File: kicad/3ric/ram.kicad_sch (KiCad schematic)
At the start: 7 parts

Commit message: update schematics
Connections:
- net CD0: now also U_BUS_DATA_?.18 (B0); no longer U_BUS_DATA_?.2 (A0)
- net CD1: now also U_BUS_DATA_?.17 (B1); no longer U_BUS_DATA_?.3 (A1)
- net CD2: now also U_BUS_DATA_?.16 (B2); no longer U_BUS_DATA_?.4 (A2)
- net CD3: now also U_BUS_DATA_?.15 (B3); no longer U_BUS_DATA_?.5 (A3)
- net CD4: now also U_BUS_DATA_?.14 (B4); no longer U_BUS_DATA_?.6 (A4)
- net CD5: now also U_BUS_DATA_?.13 (B5); no longer U_BUS_DATA_?.7 (A5)
- net CD6: now also U_BUS_DATA_?.12 (B6); no longer U_BUS_DATA_?.8 (A6)
- net CD7: now also U_BUS_DATA_?.11 (B7); no longer U_BUS_DATA_?.9 (A7)
- net VD0: now also U_BUS_DATA_?.2 (A0); no longer U_BUS_DATA_?.18 (B0)
- net VD1: now also U_BUS_DATA_?.3 (A1); no longer U_BUS_DATA_?.17 (B1)
- net VD2: now also U_BUS_DATA_?.4 (A2); no longer U_BUS_DATA_?.16 (B2)
- net VD3: now also U_BUS_DATA_?.5 (A3); no longer U_BUS_DATA_?.15 (B3)
- net VD4: now also U_BUS_DATA_?.6 (A4); no longer U_BUS_DATA_?.14 (B4)
- net VD5: now also U_BUS_DATA_?.7 (A5); no longer U_BUS_DATA_?.13 (B5)
- net VD6: now also U_BUS_DATA_?.8 (A6); no longer U_BUS_DATA_?.12 (B6)
- net VD7: now also U_BUS_DATA_?.9 (A7); no longer U_BUS_DATA_?.11 (B7)
- net VL0: now also U_VDATA_LATCH?.19 (Q0); no longer U_VDATA_LATCH?.12 (Q7)
- net VL1: now also U_VDATA_LATCH?.18 (Q1); no longer U_VDATA_LATCH?.13 (Q6)
- net VL2: now also U_VDATA_LATCH?.17 (Q2); no longer U_VDATA_LATCH?.14 (Q5)
- net VL3: now also U_VDATA_LATCH?.16 (Q3); no longer U_VDATA_LATCH?.15 (Q4)
- net VL4: now also U_VDATA_LATCH?.15 (Q4); no longer U_VDATA_LATCH?.16 (Q3)
- net VL5: now also U_VDATA_LATCH?.14 (Q5); no longer U_VDATA_LATCH?.17 (Q2)
- net VL6: now also U_VDATA_LATCH?.13 (Q6); no longer U_VDATA_LATCH?.18 (Q1)
- net VL7: now also U_VDATA_LATCH?.12 (Q7); no longer U_VDATA_LATCH?.19 (Q0)
- net VIDENABLE renamed VIDENABLE2

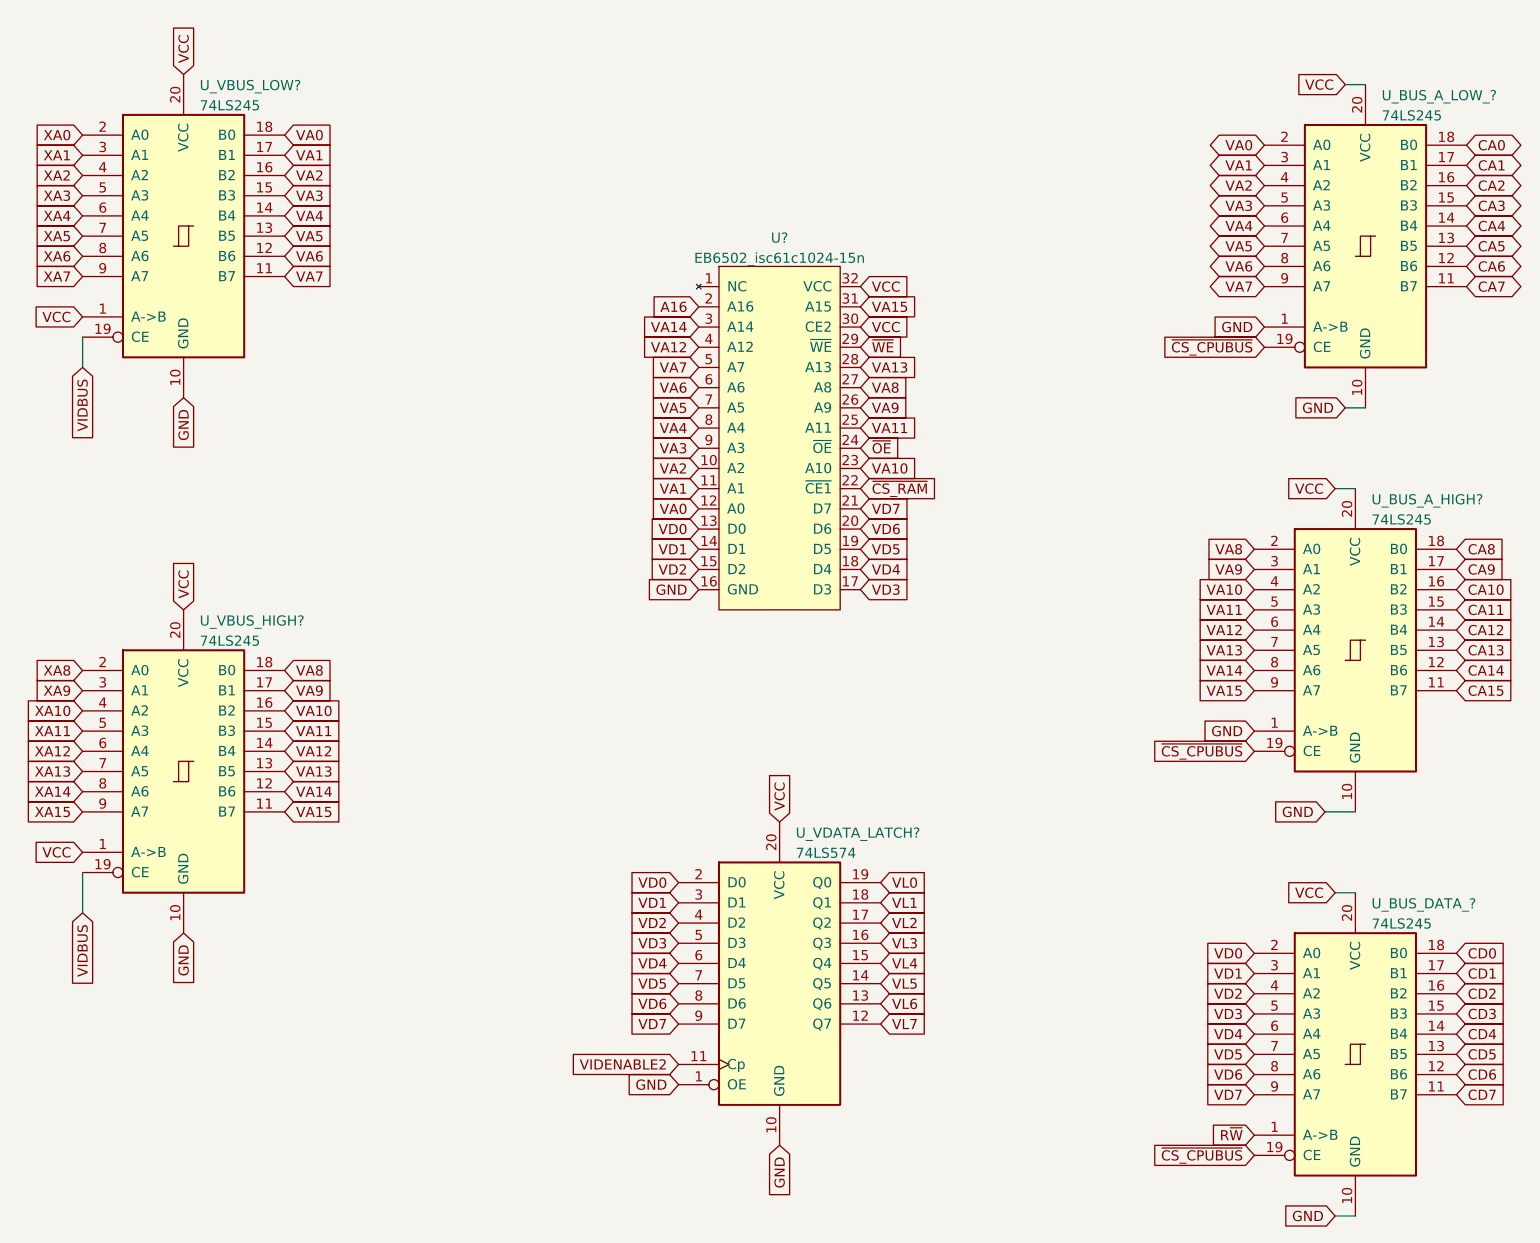
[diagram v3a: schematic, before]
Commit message: update schematic based on breadboard
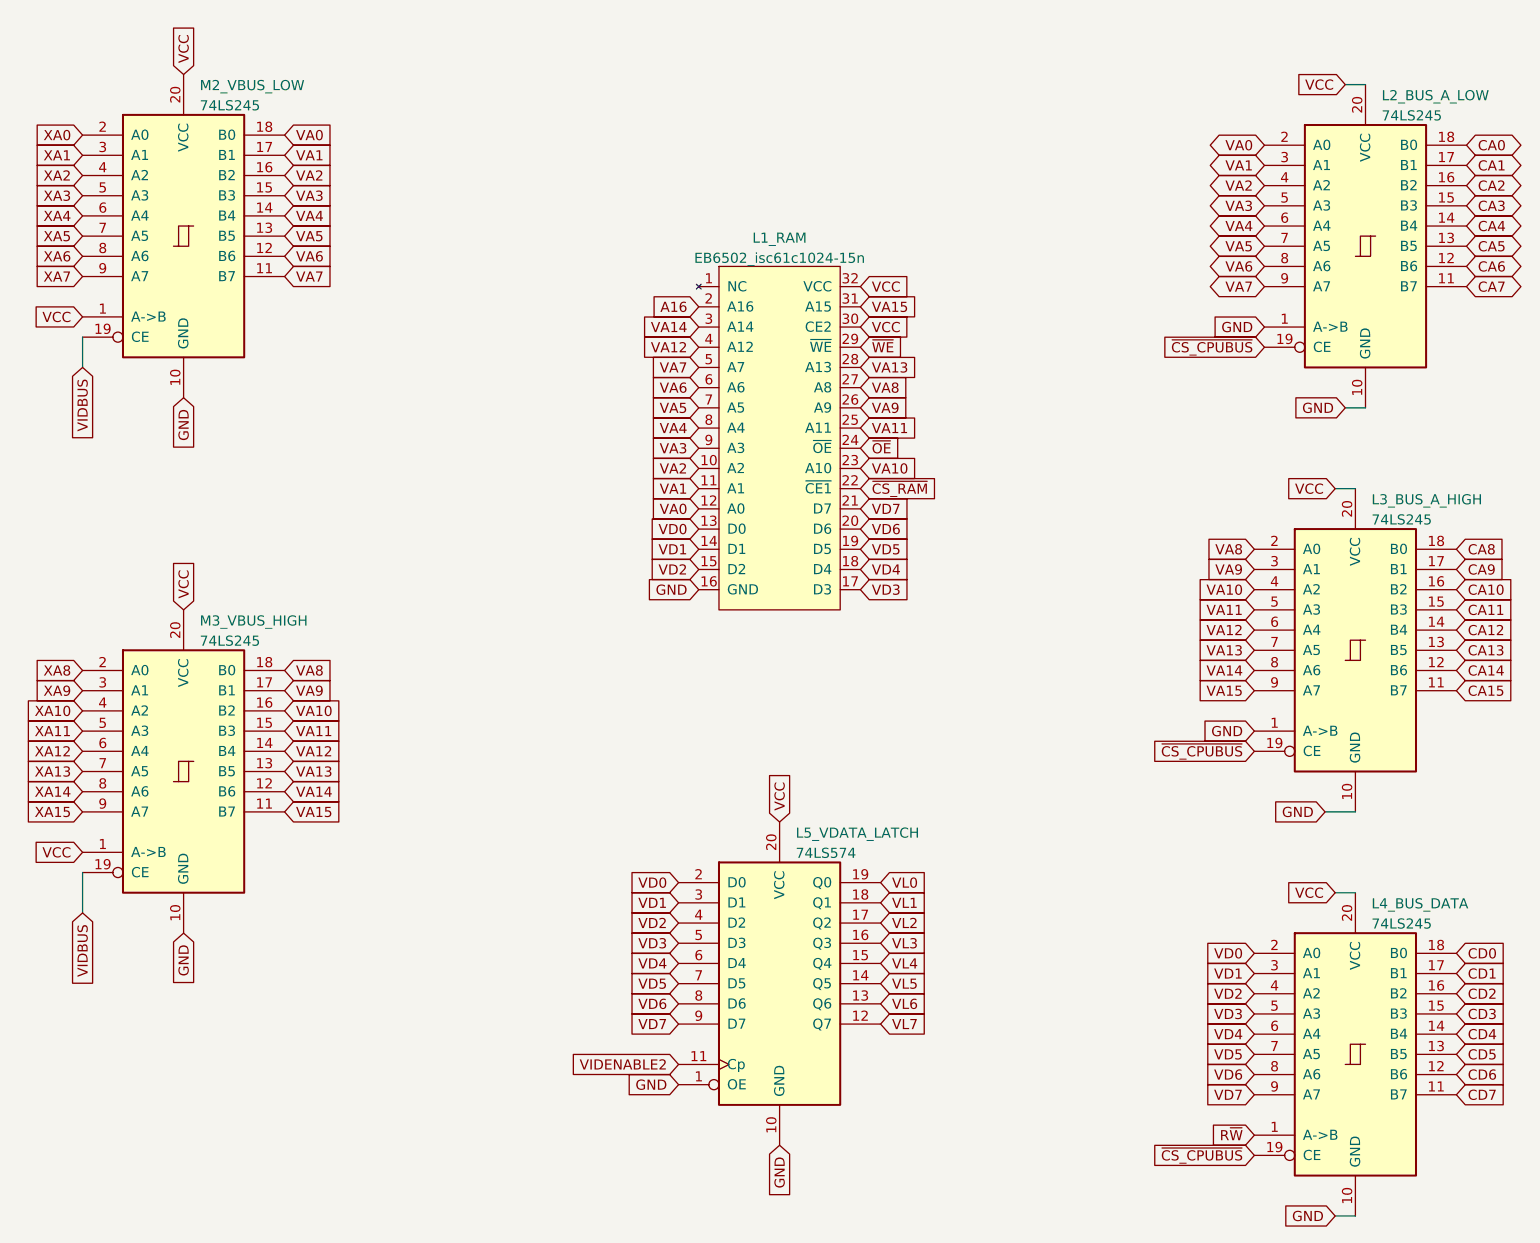
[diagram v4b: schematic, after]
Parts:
- gave numbers to parts that had none: 7
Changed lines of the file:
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@@
 		(dnp no)
 		(fields_autoplaced yes)
-		(property "Reference" "U_VBUS_LOW?"
+		(property "Reference" "M2_VBUS_LOW"
 			(at 59.1694 19.1602 0)
 			(effects
@@
 			(project "3ric"
 				(path "/e63e39d7-6ac0-4ffd-8aa3-1841a4541b55/24a3ac67-b632-4551-8167-d5cda39cc266"
-					(reference "U_VBUS_LOW?")
+					(reference "M2_VBUS_LOW")
 					(unit 1)
 				)
@@
 		(dnp no)
 		(fields_autoplaced yes)
-		(property "Reference" "U_BUS_A_HIGH?"
+		(property "Reference" "L3_BUS_A_HIGH"
 			(at 206.4894 71.2302 0)
 			(effects
@@
 			(project "3ric"
 				(path "/e63e39d7-6ac0-4ffd-8aa3-1841a4541b55/24a3ac67-b632-4551-8167-d5cda39cc266"
-					(reference "U_BUS_A_HIGH?")
+					(reference "L3_BUS_A_HIGH")
 					(unit 1)
 				)
@@
 		(dnp no)
 		(fields_autoplaced yes)
-		(property "Reference" "U_BUS_A_LOW_?"
+		(property "Reference" "L2_BUS_A_LOW"
 			(at 207.7594 20.4302 0)
 			(effects
@@
 			(project "3ric"
 				(path "/e63e39d7-6ac0-4ffd-8aa3-1841a4541b55/24a3ac67-b632-4551-8167-d5cda39cc266"
-					(reference "U_BUS_A_LOW_?")
+					(reference "L2_BUS_A_LOW")
 					(unit 1)
 				)
@@
 		(dnp no)
 		(fields_autoplaced yes)
-		(property "Reference" "U?"
+		(property "Reference" "L1_RAM"
 			(at 132.08 38.3372 0)
 			(effects
@@
 			(project "3ric"
 				(path "/e63e39d7-6ac0-4ffd-8aa3-1841a4541b55/24a3ac67-b632-4551-8167-d5cda39cc266"
-					(reference "U?")
+					(reference "L1_RAM")
 					(unit 1)
 				)
@@
 		(dnp no)
 		(fields_autoplaced yes)
-		(property "Reference" "U_BUS_DATA_?"
+		(property "Reference" "L4_BUS_DATA"
 			(at 206.4894 122.0302 0)
 			(effects
@@
 			(project "3ric"
 				(path "/e63e39d7-6ac0-4ffd-8aa3-1841a4541b55/24a3ac67-b632-4551-8167-d5cda39cc266"
-					(reference "U_BUS_DATA_?")
+					(reference "L4_BUS_DATA")
 					(unit 1)
 				)
@@
 		(dnp no)
 		(fields_autoplaced yes)
-		(property "Reference" "U_VDATA_LATCH?"
+		(property "Reference" "L5_VDATA_LATCH"
 			(at 134.0994 113.1402 0)
 			(effects
@@
 			(project "3ric"
 				(path "/e63e39d7-6ac0-4ffd-8aa3-1841a4541b55/24a3ac67-b632-4551-8167-d5cda39cc266"
-					(reference "U_VDATA_LATCH?")
+					(reference "L5_VDATA_LATCH")
 					(unit 1)
 				)
@@
 		(dnp no)
 		(fields_autoplaced yes)
-		(property "Reference" "U_VBUS_HIGH?"
+		(property "Reference" "M3_VBUS_HIGH"
 			(at 59.1694 86.4702 0)
 			(effects
@@
 			(project "3ric"
 				(path "/e63e39d7-6ac0-4ffd-8aa3-1841a4541b55/24a3ac67-b632-4551-8167-d5cda39cc266"
-					(reference "U_VBUS_HIGH?")
+					(reference "M3_VBUS_HIGH")
 					(unit 1)
 				)

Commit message: cleaning up of the schematic
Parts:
- renumbered L1_RAM to L1_RAM1, L2_BUS_A_LOW to L2_BUS_A_LOW1, L3_BUS_A_HIGH to L3_BUS_A_HIGH1, L4_BUS_DATA to L4_BUS_DATA1, L5_VDATA_LATCH to L5_VDATA_LATCH1, M2_VBUS_LOW to M2_VBUS_LOW1, M3_VBUS_HIGH to M3_VBUS_HIGH1
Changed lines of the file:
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@@
 		(dnp no)
 		(fields_autoplaced yes)
-		(property "Reference" "M2_VBUS_LOW"
+		(property "Reference" "M2_VBUS_LOW1"
 			(at 59.1694 19.1602 0)
 			(effects
@@
 			(project "3ric"
 				(path "/e63e39d7-6ac0-4ffd-8aa3-1841a4541b55/24a3ac67-b632-4551-8167-d5cda39cc266"
-					(reference "M2_VBUS_LOW")
+					(reference "M2_VBUS_LOW1")
 					(unit 1)
 				)
@@
 		(dnp no)
 		(fields_autoplaced yes)
-		(property "Reference" "L3_BUS_A_HIGH"
+		(property "Reference" "L3_BUS_A_HIGH1"
 			(at 206.4894 71.2302 0)
 			(effects
@@
 			(project "3ric"
 				(path "/e63e39d7-6ac0-4ffd-8aa3-1841a4541b55/24a3ac67-b632-4551-8167-d5cda39cc266"
-					(reference "L3_BUS_A_HIGH")
+					(reference "L3_BUS_A_HIGH1")
 					(unit 1)
 				)
@@
 		(dnp no)
 		(fields_autoplaced yes)
-		(property "Reference" "L2_BUS_A_LOW"
+		(property "Reference" "L2_BUS_A_LOW1"
 			(at 207.7594 20.4302 0)
 			(effects
@@
 			(project "3ric"
 				(path "/e63e39d7-6ac0-4ffd-8aa3-1841a4541b55/24a3ac67-b632-4551-8167-d5cda39cc266"
-					(reference "L2_BUS_A_LOW")
+					(reference "L2_BUS_A_LOW1")
 					(unit 1)
 				)
@@
 		(dnp no)
 		(fields_autoplaced yes)
-		(property "Reference" "L1_RAM"
+		(property "Reference" "L1_RAM1"
 			(at 132.08 38.3372 0)
 			(effects
@@
 			(project "3ric"
 				(path "/e63e39d7-6ac0-4ffd-8aa3-1841a4541b55/24a3ac67-b632-4551-8167-d5cda39cc266"
-					(reference "L1_RAM")
+					(reference "L1_RAM1")
 					(unit 1)
 				)
@@
 		(dnp no)
 		(fields_autoplaced yes)
-		(property "Reference" "L4_BUS_DATA"
+		(property "Reference" "L4_BUS_DATA1"
 			(at 206.4894 122.0302 0)
 			(effects
@@
 			(project "3ric"
 				(path "/e63e39d7-6ac0-4ffd-8aa3-1841a4541b55/24a3ac67-b632-4551-8167-d5cda39cc266"
-					(reference "L4_BUS_DATA")
+					(reference "L4_BUS_DATA1")
 					(unit 1)
 				)
@@
 		(dnp no)
 		(fields_autoplaced yes)
-		(property "Reference" "L5_VDATA_LATCH"
+		(property "Reference" "L5_VDATA_LATCH1"
 			(at 134.0994 113.1402 0)
 			(effects
@@
 			(project "3ric"
 				(path "/e63e39d7-6ac0-4ffd-8aa3-1841a4541b55/24a3ac67-b632-4551-8167-d5cda39cc266"
-					(reference "L5_VDATA_LATCH")
+					(reference "L5_VDATA_LATCH1")
 					(unit 1)
 				)
@@
 		(dnp no)
 		(fields_autoplaced yes)
-		(property "Reference" "M3_VBUS_HIGH"
+		(property "Reference" "M3_VBUS_HIGH1"
 			(at 59.1694 86.4702 0)
 			(effects
@@
 			(project "3ric"
 				(path "/e63e39d7-6ac0-4ffd-8aa3-1841a4541b55/24a3ac67-b632-4551-8167-d5cda39cc266"
-					(reference "M3_VBUS_HIGH")
+					(reference "M3_VBUS_HIGH1")
 					(unit 1)
 				)

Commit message: pcb layout continued
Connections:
- net CD0: now also L4_BUS_DATA1.11 (B7); no longer L4_BUS_DATA1.18 (B0)
- net CD1: now also L4_BUS_DATA1.12 (B6); no longer L4_BUS_DATA1.17 (B1)
- net CD2: now also L4_BUS_DATA1.13 (B5); no longer L4_BUS_DATA1.16 (B2)
- net CD3: now also L4_BUS_DATA1.14 (B4); no longer L4_BUS_DATA1.15 (B3)
- net CD4: now also L4_BUS_DATA1.15 (B3); no longer L4_BUS_DATA1.14 (B4)
- net CD5: now also L4_BUS_DATA1.16 (B2); no longer L4_BUS_DATA1.13 (B5)
- net CD6: now also L4_BUS_DATA1.17 (B1); no longer L4_BUS_DATA1.12 (B6)
- net CD7: now also L4_BUS_DATA1.18 (B0); no longer L4_BUS_DATA1.11 (B7)
- net VD0: now also L4_BUS_DATA1.9 (A7), L5_VDATA_LATCH1.9 (D7); no longer L4_BUS_DATA1.2 (A0), L5_VDATA_LATCH1.2 (D0)
- net VD1: now also L4_BUS_DATA1.8 (A6), L5_VDATA_LATCH1.8 (D6); no longer L4_BUS_DATA1.3 (A1), L5_VDATA_LATCH1.3 (D1)
- net VD2: now also L4_BUS_DATA1.7 (A5), L5_VDATA_LATCH1.7 (D5); no longer L4_BUS_DATA1.4 (A2), L5_VDATA_LATCH1.4 (D2)
- net VD3: now also L4_BUS_DATA1.6 (A4), L5_VDATA_LATCH1.6 (D4); no longer L4_BUS_DATA1.5 (A3), L5_VDATA_LATCH1.5 (D3)
- net VD4: now also L4_BUS_DATA1.5 (A3), L5_VDATA_LATCH1.5 (D3); no longer L4_BUS_DATA1.6 (A4), L5_VDATA_LATCH1.6 (D4)
- net VD5: now also L4_BUS_DATA1.4 (A2), L5_VDATA_LATCH1.4 (D2); no longer L4_BUS_DATA1.7 (A5), L5_VDATA_LATCH1.7 (D5)
- net VD6: now also L4_BUS_DATA1.3 (A1), L5_VDATA_LATCH1.3 (D1); no longer L4_BUS_DATA1.8 (A6), L5_VDATA_LATCH1.8 (D6)
- net VD7: now also L4_BUS_DATA1.2 (A0), L5_VDATA_LATCH1.2 (D0); no longer L4_BUS_DATA1.9 (A7), L5_VDATA_LATCH1.9 (D7)
- net VL0: now also L5_VDATA_LATCH1.12 (Q7); no longer L5_VDATA_LATCH1.19 (Q0)
- net VL1: now also L5_VDATA_LATCH1.13 (Q6); no longer L5_VDATA_LATCH1.18 (Q1)
- net VL2: now also L5_VDATA_LATCH1.14 (Q5); no longer L5_VDATA_LATCH1.17 (Q2)
- net VL3: now also L5_VDATA_LATCH1.15 (Q4); no longer L5_VDATA_LATCH1.16 (Q3)
- net VL4: now also L5_VDATA_LATCH1.16 (Q3); no longer L5_VDATA_LATCH1.15 (Q4)
- net VL5: now also L5_VDATA_LATCH1.17 (Q2); no longer L5_VDATA_LATCH1.14 (Q5)
- net VL6: now also L5_VDATA_LATCH1.18 (Q1); no longer L5_VDATA_LATCH1.13 (Q6)
- net VL7: now also L5_VDATA_LATCH1.19 (Q0); no longer L5_VDATA_LATCH1.12 (Q7)
